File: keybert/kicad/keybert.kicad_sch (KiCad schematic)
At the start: 50 parts, among them J0 TRRS

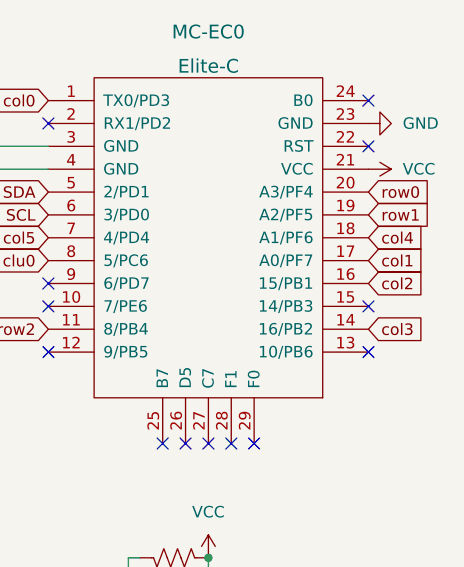
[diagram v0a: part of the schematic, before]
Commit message: fix: new revision to reduce costs
Having followed the
[Aisler design rules](https://aisler.community/t/pcb-design-rules/41)
I think this new design should be cheaper
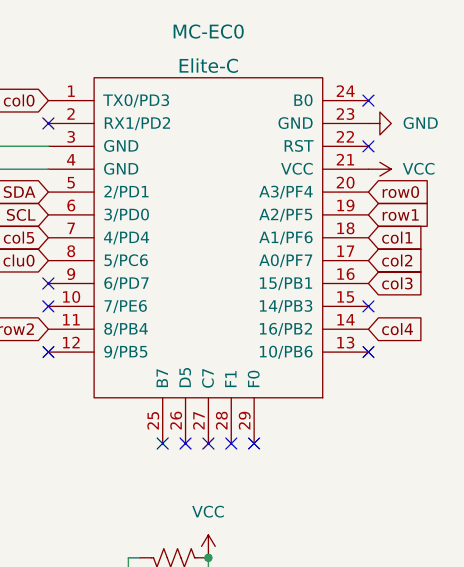
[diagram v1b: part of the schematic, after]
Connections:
- net col1: now also MC-EC0.18 (A1/PF6); no longer MC-EC0.17 (A0/PF7)
- net col2: now also MC-EC0.17 (A0/PF7); no longer MC-EC0.16 (15/PB1)
- net col3: now also MC-EC0.16 (15/PB1); no longer MC-EC0.14 (16/PB2)
- net col4: now also MC-EC0.14 (16/PB2); no longer MC-EC0.18 (A1/PF6)
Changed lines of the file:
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@@
     )
   )
-  (global_label "col4" (shape input) (at 170.18 36.83 0) (fields_autoplaced)
+  (global_label "col1" (shape input) (at 170.18 36.83 0) (fields_autoplaced)
     (effects (font (size 1.27 1.27)) (justify left))
     (property "Intersheet References" "${INTERSHEET_REFS}" (id 0) (at 176.7055 36.7506 0)
@@
     )
   )
-  (global_label "col2" (shape input) (at 170.18 41.91 0) (fields_autoplaced)
+  (global_label "col3" (shape input) (at 170.18 41.91 0) (fields_autoplaced)
     (effects (font (size 1.27 1.27)) (justify left))
     (property "Intersheet References" "${INTERSHEET_REFS}" (id 0) (at 176.7055 41.8306 0)
@@
     )
   )
-  (global_label "col1" (shape input) (at 170.18 39.37 0) (fields_autoplaced)
+  (global_label "col2" (shape input) (at 170.18 39.37 0) (fields_autoplaced)
     (effects (font (size 1.27 1.27)) (justify left))
     (property "Intersheet References" "${INTERSHEET_REFS}" (id 0) (at 176.7055 39.2906 0)
@@
     )
   )
-  (global_label "col3" (shape input) (at 170.18 46.99 0) (fields_autoplaced)
+  (global_label "col4" (shape input) (at 170.18 46.99 0) (fields_autoplaced)
     (effects (font (size 1.27 1.27)) (justify left))
     (property "Intersheet References" "${INTERSHEET_REFS}" (id 0) (at 176.7055 46.9106 0)

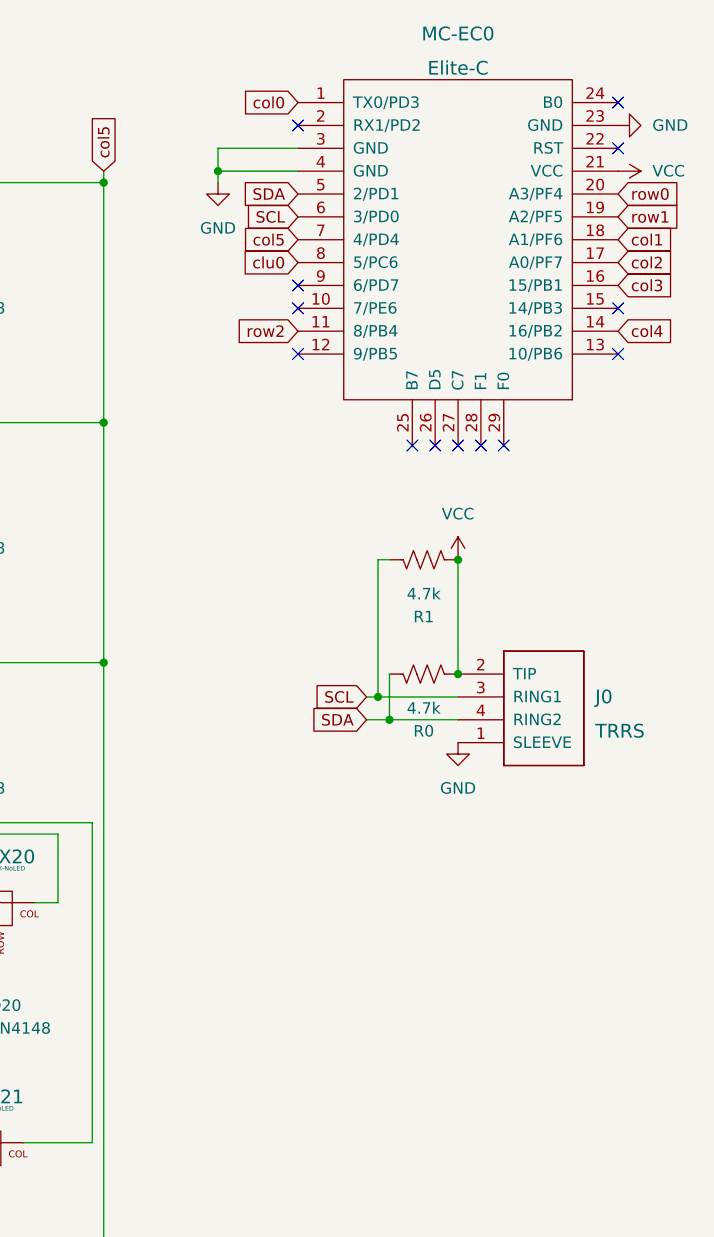
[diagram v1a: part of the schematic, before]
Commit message: fix: No longer incurring complexity fee
After a lot of work, the PCB itself should now be viable for ordering.
At time of completion of that work, the PCB is $30 to be produced in the
United states in a batch of 3 or $22 to be produced in China in a batch
of 5. Arguably, that batch of five is more in line with the vision for
Keybert, however, I would forsee myself preferring the American PCB
manufacturer for my own boards given overall sociopolitical
circumstances in the world. I have decided that Keybert will exist
purely in the cheapest possible way with no guidance on how ethical or
unethical it is to engage with various entities. There likely will need
to be documentation somewhere stating outright that the creator of
Keybert in no way condones things like the Uigher genocide, the invasion
of Ukraine, or any other form of genocide

fix: added library file for TRRS jack

In order to properly work with the Keebio TRRS symbol, I needed to
create a footprint that matched it in terms of pads. Or wait no.
Otherway. I wanted to use the Keebio footprint, so I created a new
symbol to match in terms of pads
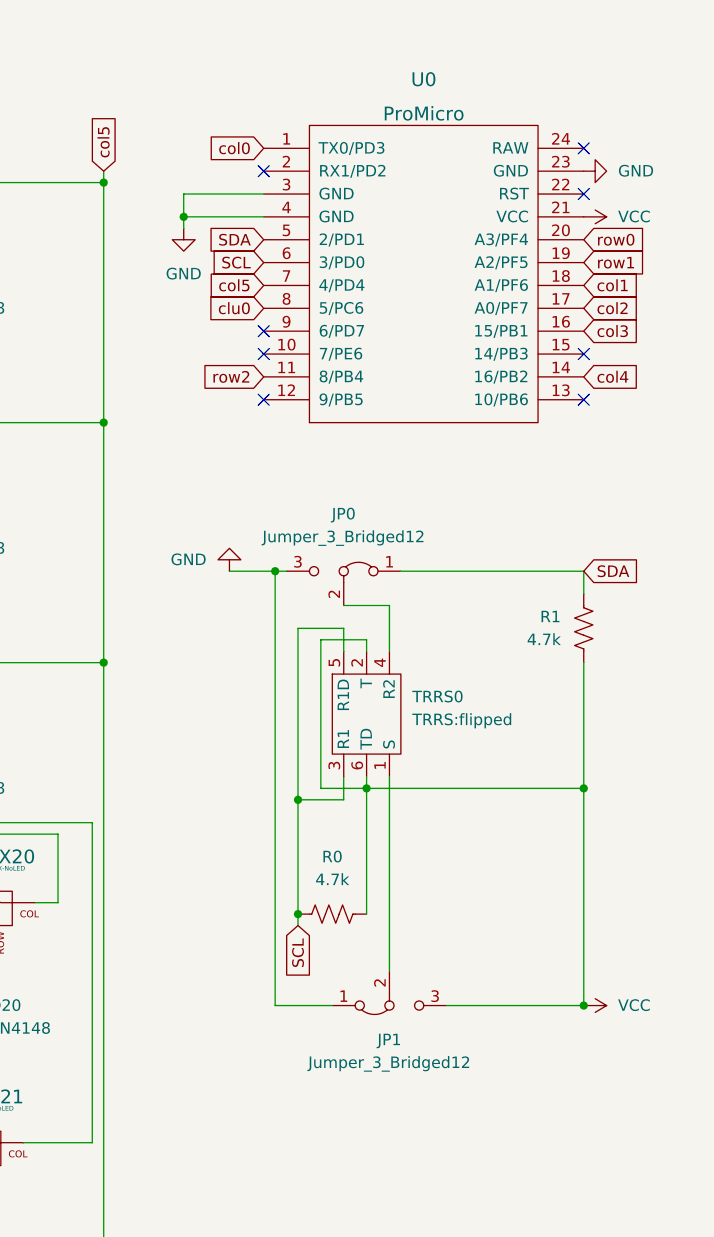
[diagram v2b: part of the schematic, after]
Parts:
- removed J0: TRRS, Keebio-Parts:TRRS-PJ-320A-dual, symbol keebio:TRRS
- removed MC-EC0: Elite-C, Keebio-Parts:Elite-C-castellated-29pin-holes, symbol keebio:Elite-C
- added JP0, JP1: Jumper_3_Bridged12, Connector_PinHeader_2.54mm:PinHeader_1x03_P2.54mm_Vertical, symbol Jumper:Jumper_3_Bridged12
- added TRRS0: TRRS:flipped, Keebio-Parts:TRRS_Jack, symbol infill-symbols:TRRS{colon}flipped
- added U0: ProMicro, Keebio-Parts:ArduinoProMicro, symbol keebio:ProMicro
- D0, D1, D10, D11, D12, D13, D14, D15, D16, D17, D18, D19, D2, D20, D21, D22, D3, D4, D5, D6, D7, D8, D9: footprint Keebio-Parts:Diode-dual -> Keebio-Parts:Diode
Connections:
- net GND: now also JP0.3 (B), JP1.1 (A), U0.23 (GND), U0.3 (GND), U0.4 (GND)
- net SCL: now also R0.2, TRRS0.3 (R1), TRRS0.5 (R1D), U0.6 (3/PD0); no longer R1.1
- net SDA: now also R1.1, JP0.1 (A), U0.5 (2/PD1); no longer R0.1
- net VCC: now also R0.1, JP1.3 (B), TRRS0.2 (T), TRRS0.6 (TD), U0.21 (VCC); no longer R0.2
- net clu0: now also U0.8 (5/PC6)
- net col0: now also U0.1 (TX0/PD3)
- net col1: now also U0.18 (A1/PF6)
- net col2: now also U0.17 (A0/PF7)
- net col3: now also U0.16 (15/PB1)
- net col4: now also U0.14 (16/PB2)
- net col5: now also U0.7 (4/PD4)
- net row0: now also U0.20 (A3/PF4)
- net row1: now also U0.19 (A2/PF5)
- net row2: now also U0.11 (8/PB4)
- new net: JP0.2 (C), TRRS0.4 (R2)
- new net: JP1.2 (C), TRRS0.1 (S)
- no-connect marks 13 -> 8

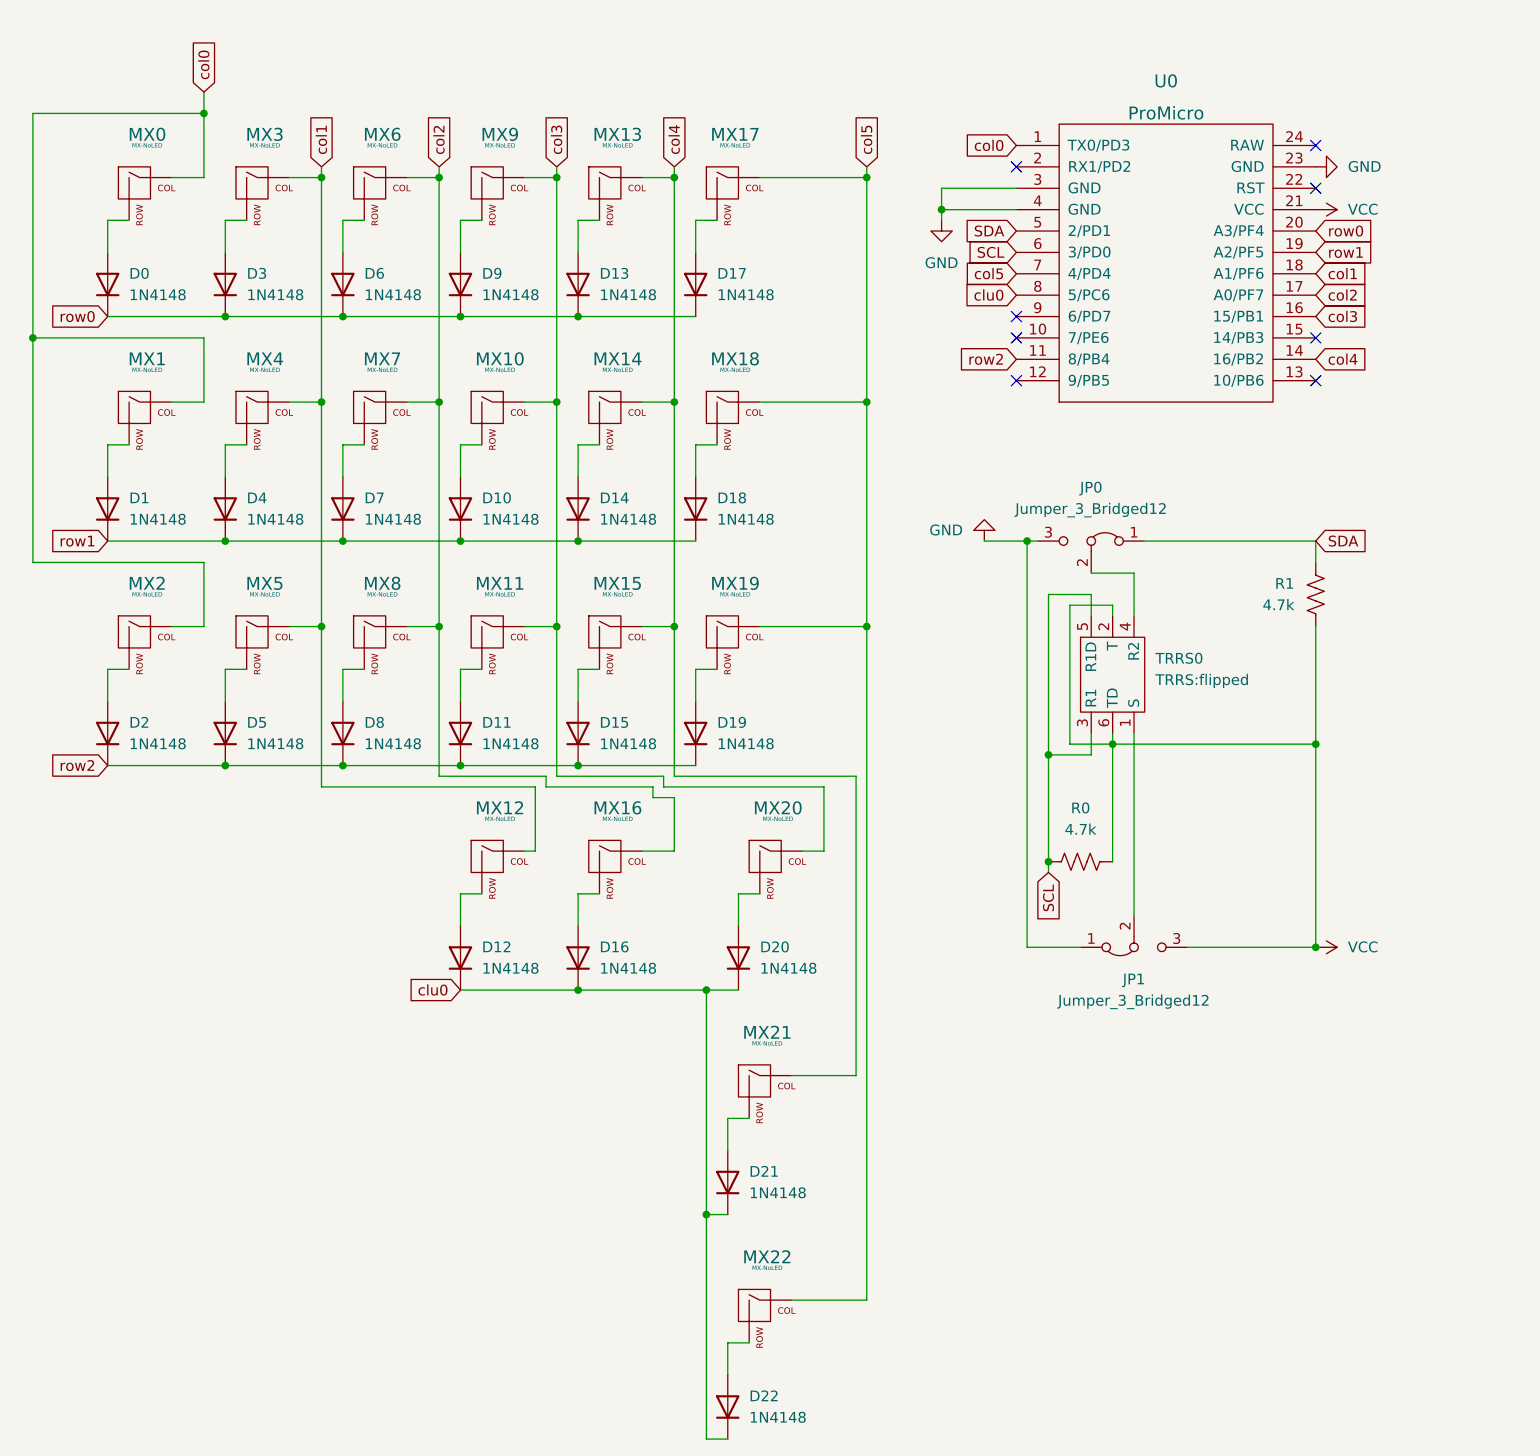
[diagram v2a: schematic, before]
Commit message: fix: redid PCB due to switch spacing issue
The spacing of the switches was all wrong I discovered upon loading up
the switch plate into FreeCAD. I've redone the basic arrangement of all
electronic parts, but the parts all need, once more to be reconnected.

I also simplified the schematic slightly. I don't like crossed wires
even though the ones that do connect are pretty clear thanks to their
green nodes
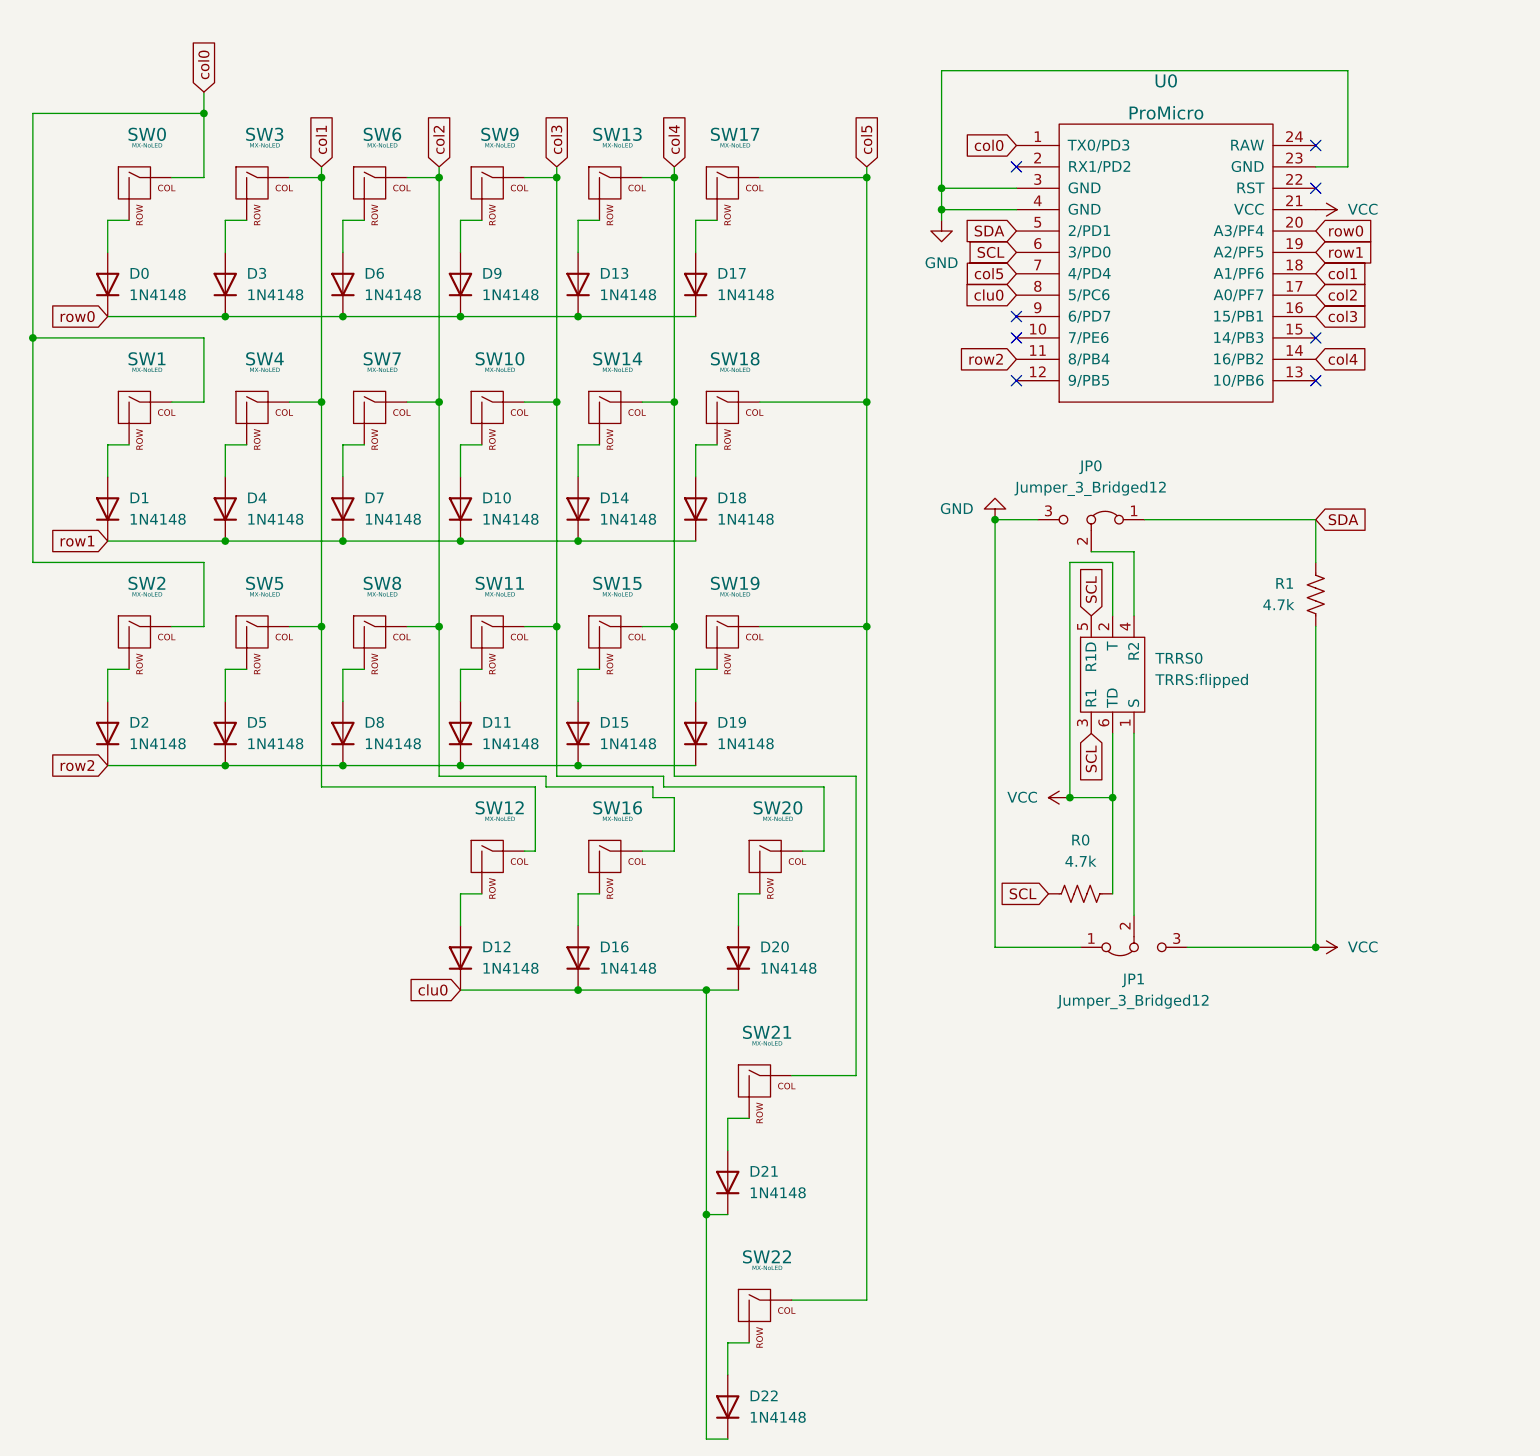
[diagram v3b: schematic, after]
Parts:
- renumbered MX0 to SW0, MX1 to SW1, MX10 to SW10, MX11 to SW11, MX12 to SW12, MX13 to SW13, MX14 to SW14, MX15 to SW15, MX16 to SW16, MX17 to SW17, MX18 to SW18, MX19 to SW19, MX2 to SW2, MX20 to SW20, MX21 to SW21, MX22 to SW22, MX3 to SW3, MX4 to SW4, MX5 to SW5, MX6 to SW6, MX7 to SW7, MX8 to SW8, MX9 to SW9
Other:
- moved on the sheet: JP0, R0
